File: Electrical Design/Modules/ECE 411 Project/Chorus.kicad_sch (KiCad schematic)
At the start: 45 parts, among them Q2 2N3904, Q3 2N3904, Q4 2N3904, U3 MN3207

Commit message: update kicad
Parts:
- V3207D1, V3207D2: On Hand (On Way) (none) -> 8; Part Number (none) -> IC-400-1033
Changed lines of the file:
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@@
 		(at 218.44 53.34)
 	)
+	(bus_entry
+		(at 234.95 2.54)
+		(size 2.54 2.54)
+		(stroke
+			(width 0)
+			(type default)
+		)
+	)
 	(wire
 		(pts
@@
 			)
 		)
-		(property "Part Number" ""
+		(property "Part Number" "IC-400-1033"
 			(at 148.59 146.05 0)
 			(effects
@@
 			)
 		)
-		(property "On Hand (On Way)" ""
+		(property "On Hand (On Way)" "8"
 			(at 148.59 146.05 0)
 			(effects
@@
 			)
 		)
-		(property "Part Number" ""
+		(property "Part Number" "IC-400-1033"
 			(at 105.41 44.45 0)
 			(effects
@@
 			)
 		)
-		(property "On Hand (On Way)" ""
+		(property "On Hand (On Way)" "8"
 			(at 105.41 44.45 0)
 			(effects

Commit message: pcb amp revision
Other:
- moved on the sheet: C1, C10, C11, C12, C13, C14, C15, C16, C17, C18, C19, C20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

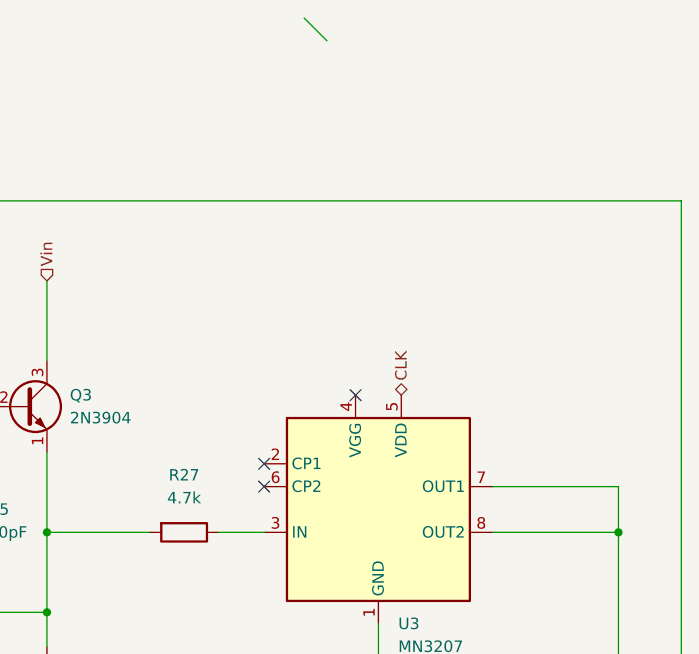
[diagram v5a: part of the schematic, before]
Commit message: adding chorus test poiunts, touch ups
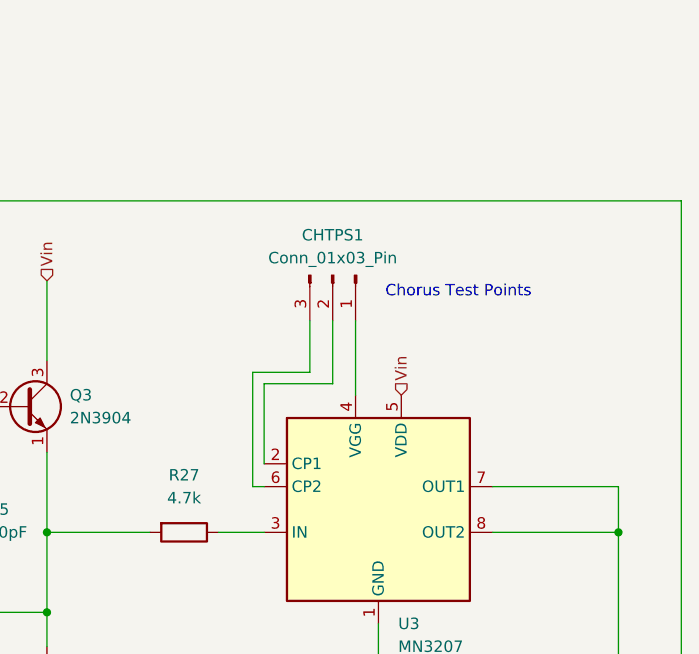
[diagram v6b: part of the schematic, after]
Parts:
- added CHTPS1: Conn_01x03_Pin, Connector_PinSocket_2.54mm:PinSocket_1x03_P2.54mm_Vertical, symbol Connector:Conn_01x03_Pin
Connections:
- net CLK is gone; now on net Vin: U3.5 (VDD)
- net at U3.2 (CP1): now also CHTPS1.2 (Pin_2)
- net at U3.4 (VGG): now also CHTPS1.1 (Pin_1)
- net at U3.6 (CP2): now also CHTPS1.3 (Pin_3)
- no-connect marks 3 -> 0
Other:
- note added: "Chorus Test Points"
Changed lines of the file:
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@@
 	(title_block
 		(title "Chorus Effect")
-		(date "2024-11-14")
-		(rev "1.5")
+		(date "2024-11-18")
+		(rev "1.6")
 		(company "Portland State University")
 		(comment 1 "Open Source Hardware")
@@
 		(color 0 0 0 0)
 	)
-	(no_connect
-		(at 230.505 52.07)
-	)
-	(no_connect
-		(at 240.665 44.45)
-	)
-	(no_connect
-		(at 230.505 54.61)
-	)
-	(bus_entry
-		(at 234.95 2.54)
-		(size 2.54 2.54)
-		(stroke
-			(width 0)
-			(type default)
-		)
-	)
 	(wire
 		(pts
@@
 	(wire
 		(pts
+			(xy 229.235 41.91) (xy 235.585 41.91)
+		)
+		(stroke
+			(width 0)
+			(type default)
+		)
+	)
+	(wire
+		(pts
 			(xy 158.115 154.94) (xy 158.115 158.75)
 		)
@@
 	(wire
 		(pts
+			(xy 240.665 36.195) (xy 240.665 44.45)
+		)
+		(stroke
+			(width 0)
+			(type default)
+		)
+	)
+	(wire
+		(pts
 			(xy 55.245 139.7) (xy 57.785 139.7)
 		)
@@
 	(wire
 		(pts
+			(xy 230.505 54.61) (xy 229.235 54.61)
+		)
+		(stroke
+			(width 0)
+			(type default)
+		)
+	)
+	(wire
+		(pts
 			(xy 175.895 45.72) (xy 178.435 45.72)
 		)
@@
 	(wire
 		(pts
+			(xy 229.235 54.61) (xy 229.235 41.91)
+		)
+		(stroke
+			(width 0)
+			(type default)
+		)
+	)
+	(wire
+		(pts
 			(xy 194.945 45.72) (xy 198.755 45.72)
 		)
@@
 	(wire
 		(pts
+			(xy 230.505 52.07) (xy 230.505 43.18)
+		)
+		(stroke
+			(width 0)
+			(type default)
+		)
+	)
+	(wire
+		(pts
 			(xy 104.775 48.26) (xy 104.775 54.61)
 		)
@@
 	(wire
 		(pts
+			(xy 235.585 41.91) (xy 235.585 36.195)
+		)
+		(stroke
+			(width 0)
+			(type default)
+		)
+	)
+	(wire
+		(pts
+			(xy 238.125 43.18) (xy 238.125 36.195)
+		)
+		(stroke
+			(width 0)
+			(type default)
+		)
+	)
+	(wire
+		(pts
 			(xy 52.705 48.26) (xy 52.705 52.07)
 		)
@@
 	(wire
 		(pts
+			(xy 230.505 43.18) (xy 238.125 43.18)
+		)
+		(stroke
+			(width 0)
+			(type default)
+		)
+	)
+	(wire
+		(pts
 			(xy 89.535 149.86) (xy 89.535 157.48)
 		)
@@
 		)
 	)
+	(text "Chorus Test Points"
+		(exclude_from_sim no)
+		(at 252.095 33.02 0)
+		(effects
+			(font
+				(size 1.27 1.27)
+				(color 0 0 0 1)
+			)
+		)
+	)
 	(hierarchical_label "CHORUSIN"
 		(shape input)
@@
 	(hierarchical_label "Vin"
 		(shape input)
-		(at 158.115 135.89 90)
+		(at 245.745 44.45 90)
 		(fields_autoplaced yes)
 		(effects
@@
 	(hierarchical_label "Vin"
 		(shape input)
-		(at 116.205 130.81 90)
+		(at 158.115 135.89 90)
 		(fields_autoplaced yes)
 		(effects
@@
 	(hierarchical_label "Vin"
 		(shape input)
-		(at 206.375 31.75 90)
+		(at 116.205 130.81 90)
 		(fields_autoplaced yes)
 		(effects
@@
 		)
 	)
-	(hierarchical_label "V.5in"
+	(hierarchical_label "Vin"
 		(shape input)
-		(at 150.495 162.56 270)
+		(at 206.375 31.75 90)
 		(fields_autoplaced yes)
 		(effects
@@
 				(size 1.27 1.27)
 			)
-			(justify right)
+			(justify left)
 		)
 	)
 	(hierarchical_label "V.5in"
 		(shape input)
-		(at 52.705 52.07 270)
+		(at 150.495 162.56 270)
 		(fields_autoplaced yes)
 		(effects
@@
 		)
 	)
-	(hierarchical_label "CLK"
-		(shape bidirectional)
-		(at 245.745 44.45 90)
+	(hierarchical_label "V.5in"
+		(shape input)
+		(at 52.705 52.07 270)
 		(fields_autoplaced yes)
 		(effects
@@
 				(size 1.27 1.27)
 			)
-			(justify left)
+			(justify right)
 		)
 	)
@@
 					(unit 1)
 				)
+			)
+		)
+	)
+	(symbol
+		(lib_id "Connector:Conn_01x03_Pin")
+		(at 238.125 31.115 270)
+		(unit 1)
+		(exclude_from_sim no)
+		(in_bom yes)
+		(on_board yes)
+		(dnp no)
+		(fields_autoplaced yes)
+		(property "Reference" "CHTPS1"
+			(at 238.125 26.67 90)
+			(effects
+				(font
+					(size 1.27 1.27)
+				)
+			)
+		)
+		(property "Value" "Conn_01x03_Pin"
+			(at 238.125 29.21 90)
+			(effects
+				(font
+					(size 1.27 1.27)
+				)
+			)
+		)
+		(property "Footprint" "Connector_PinSocket_2.54mm:PinSocket_1x03_P2.54mm_Vertical"
+			(at 238.125 31.115 0)
+			(effects
+				(font
+					(size 1.27 1.27)
+				)
+				(hide yes)
+			)
+		)
+		(property "Datasheet" "~"
+			(at 238.125 31.115 0)
+			(effects
+				(font
+					(size 1.27 1.27)
+				)
+				(hide yes)
+			)
+		)
+		(property "Description" "Generic connector, single row, 01x03, script generated"
+			(at 238.125 31.115 0)
+			(effects
+				(font
+					(size 1.27 1.27)
+				)
+				(hide yes)
+			)
+		)
+		(pin "2"
+		)
+		(pin "3"
+		)
+		(pin "1"
+		)
+		(instances
+			(project ""
+				(path "/2625e5a1-d0c8-41ce-941d-75d035a5f1c5/9b94327a-6b02-4c1c-b4e8-ca4e897770fe"
+					(reference "CHTPS1")
+					(unit 1)
+				)

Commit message: minor formatting updates
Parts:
- C1, C10: On Hand (On Way) (100) -> (none); On_Hand_(On_Way) (none) -> (100); Part Number CL21B473KBCNNNC -> (none); Part Origin DK -> (none); Part_Number (none) -> CL21B473KBCNNNC; Part_Origin (none) -> DK
- C11: On Hand (On Way) (100) -> (none); On_Hand_(On_Way) (none) -> (100); Part Number KGM21NR71H683KT -> (none); Part Origin DK -> (none); Part_Number (none) -> KGM21NR71H683KT; Part_Origin (none) -> DK
- C12: On Hand (On Way) (100) -> (none); On_Hand_(On_Way) (none) -> (100); Part Number CL21B334KBFNNNE -> (none); Part Origin DK -> (none); Part_Number (none) -> CL21B334KBFNNNE; Part_Origin (none) -> DK
- C13, C41: On Hand (On Way) (50) -> (none); On_Hand_(On_Way) (none) -> (50); Part Number C0805C332K1RECAUTO -> (none); Part Origin DK -> (none); Part_Number (none) -> C0805C332K1RECAUTO; Part_Origin (none) -> DK
- C14, C17: On Hand (On Way) (50) -> (none); On_Hand_(On_Way) (none) -> (50); Part Number C0402C822K1RACAUTO -> (none); Part Origin DK -> (none); Part_Number (none) -> C0402C822K1RACAUTO; Part_Origin (none) -> DK
- C15, C18: On Hand (On Way) (100) -> (none); On_Hand_(On_Way) (none) -> (100); Part Number C0805C471K5RAC7800 -> (none); Part Origin DK -> (none); Part_Number (none) -> C0805C471K5RAC7800; Part_Origin (none) -> DK
- C16, C19: On Hand (On Way) (50) -> (none); On_Hand_(On_Way) (none) -> (50); Part Number C0805C333K1RECAUTO -> (none); Part Origin DK -> (none); Part_Number (none) -> C0805C333K1RECAUTO; Part_Origin (none) -> DK
- C20: On Hand (On Way) (50) -> (none); On_Hand_(On_Way) (none) -> (50); Part Number C0805C682J1GEC7210 -> (none); Part Origin DK -> (none); Part_Number (none) -> C0805C682J1GEC7210; Part_Origin (none) -> DK
- C21: On Hand (On Way) (100) -> (none); On_Hand_(On_Way) (none) -> (100); Part Number CL21B104KBCNNNC -> (none); Part Origin DK -> (none); Part_Number (none) -> CL21B104KBCNNNC; Part_Origin (none) -> DK
- R10, R16, R17, R18, R19, R20, R21, R22, R23, R24, R25, R26, R27, R28, R3, R30, R31, R32, R34, R35, R36, R37, R6, R7, R8: Part Origin DK -> (none); Part_Origin (none) -> DK
- U3: Part Origin SBP -> (none); Part_Origin (none) -> SBP
- V3207D1, V3207D2: On Hand (On Way) 8 -> (none); On_Hand_(On_Way) (none) -> 8; Part Number IC-400-1033 -> (none); Part Origin SBP -> (none); Part_Number (none) -> IC-400-1033; Part_Origin (none) -> SBP
